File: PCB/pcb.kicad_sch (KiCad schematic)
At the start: 20 parts, among them J1 USB_C_Receptacle_USB2.0, SW1 SW_Push, U1 AT90USB1286-AU, Y1 Crystal_GND24_Small

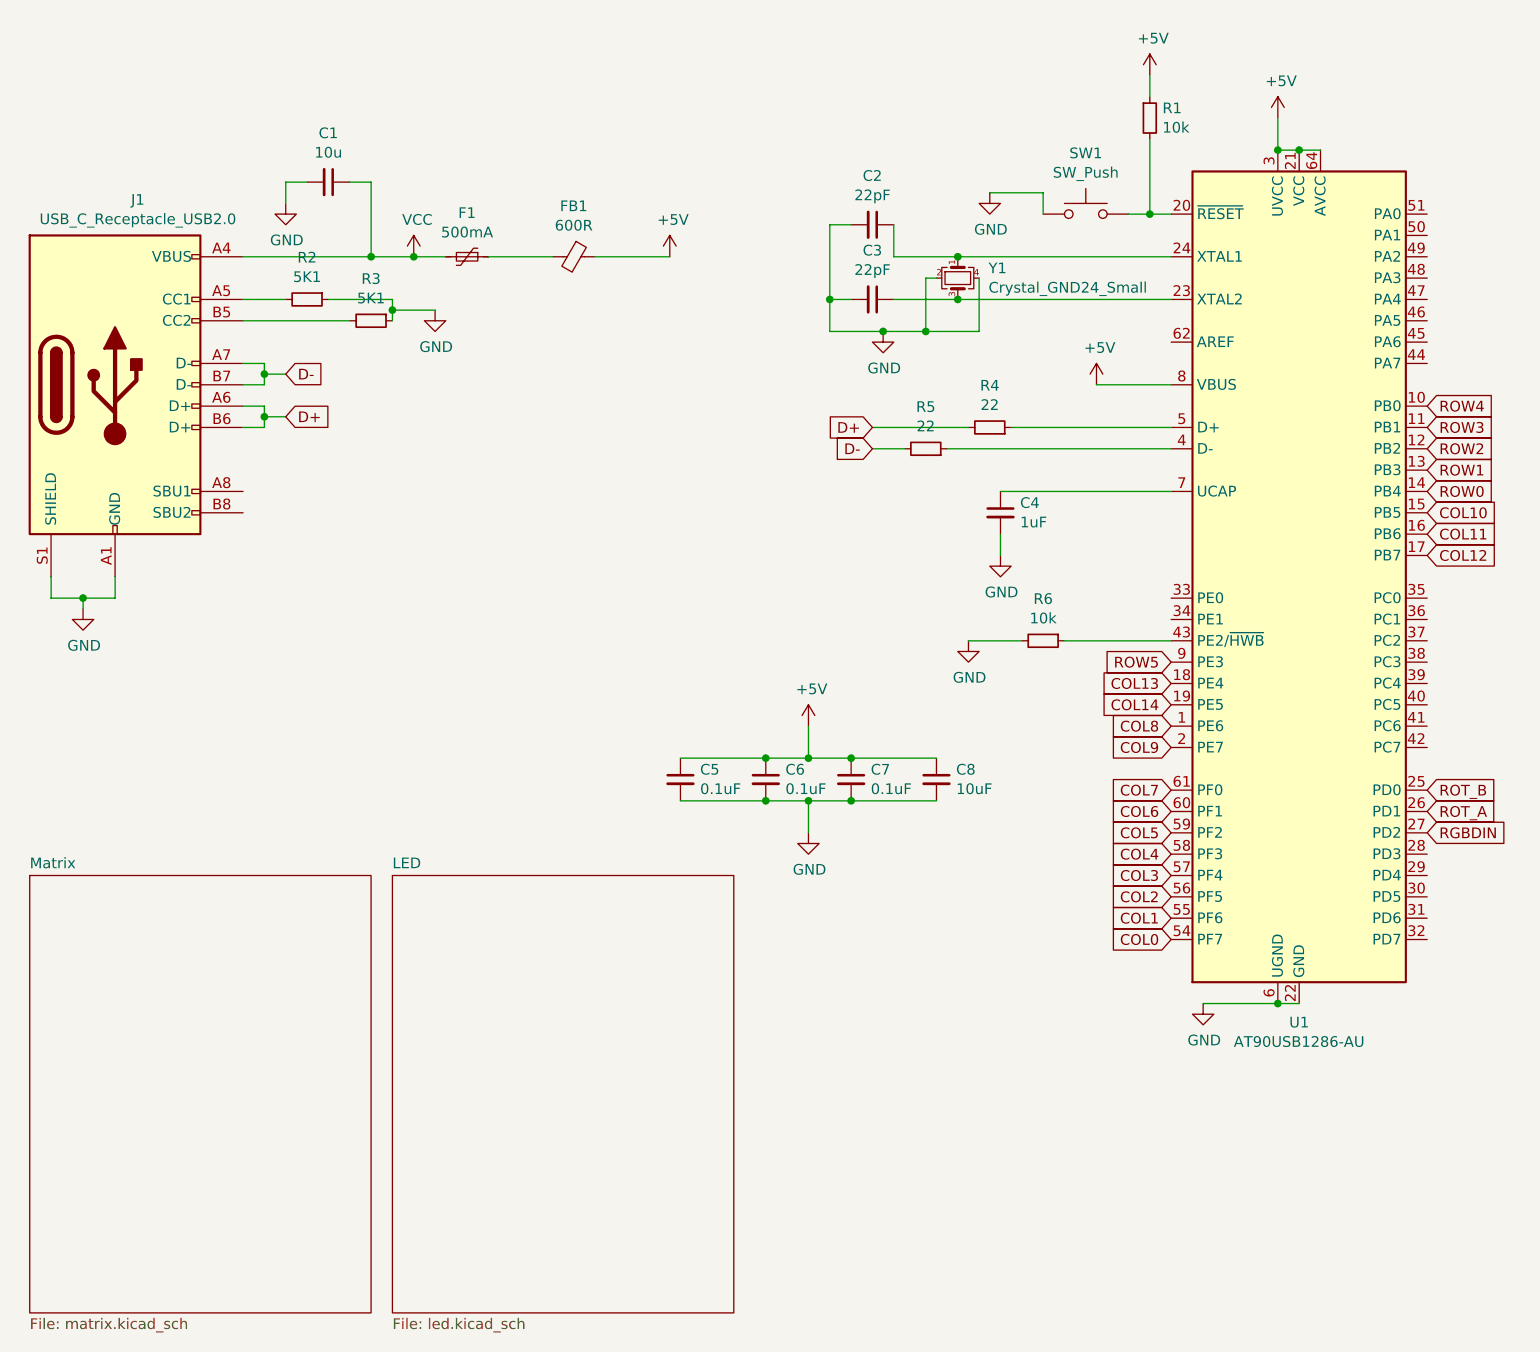
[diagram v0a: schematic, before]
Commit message: New Connector
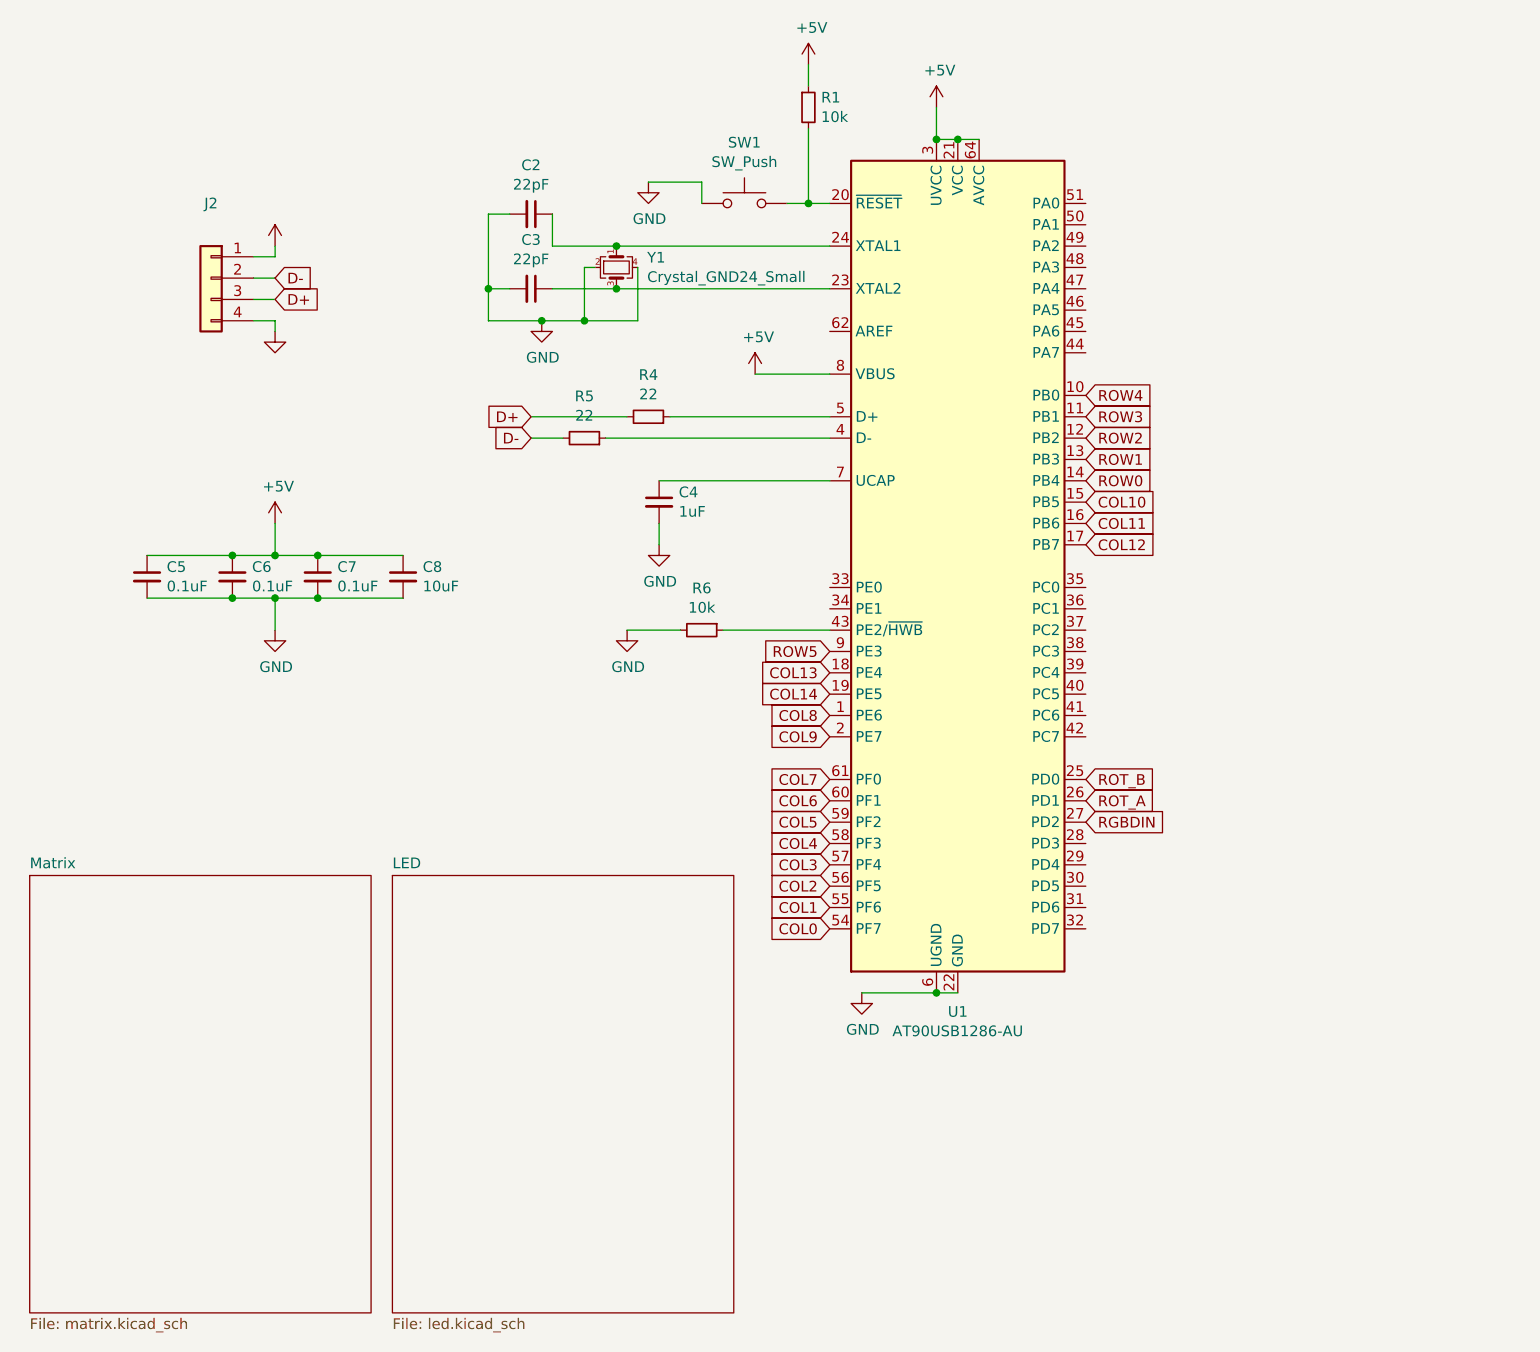
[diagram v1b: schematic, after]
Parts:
- removed C1: 10u, Capacitor_SMD:C_0805_2012Metric, symbol Device:C_Small
- removed F1: 500mA, symbol Device:Polyfuse_Small
- removed FB1: 600R, symbol pcb-rescue:Ferrite_Bead_Small-Device
- removed J1: USB_C_Receptacle_USB2.0, symbol pcb-rescue:USB_C_Receptacle_USB2.0-Connector
- removed R2, R3: 5K1, Resistor_SMD:R_0805_2012Metric, symbol Device:R_Small
- added J2: (no value), symbol Connector_Generic:Conn_01x04
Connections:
- net +5V: now also J2.1 (Pin_1)
- net D+: now also J2.3 (Pin_3)
- net D-: now also J2.2 (Pin_2)
- net GND: now also J2.4 (Pin_4)
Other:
- moved on the sheet: C2, C3, C4, C5, C6, C7, C8, R1, R4, R5, R6, SW1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

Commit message: Now only 2 alternative bottom rows
6.25U (Three 1U Keys to the right) and 7U (One 1.25U Key and one 1U Key to the right) Space Supported

Also new rounded PCB
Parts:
- J2: value (none) -> Conn_01x04; footprint (none) -> random-keyboard-parts:JST-SR-4
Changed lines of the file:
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@@
     (in_bom yes) (on_board yes) (fields_autoplaced)
     (property "Reference" "J2" (id 0) (at 38.1 38.1 0))
-    (property "Value" "" (id 1) (at 38.1 40.64 0))
-    (property "Footprint" "" (id 2) (at 38.1 46.99 0)
+    (property "Value" "Conn_01x04" (id 1) (at 38.1 40.64 0))
+    (property "Footprint" "random-keyboard-parts:JST-SR-4" (id 2) (at 38.1 46.99 0)
       (effects (font (size 1.27 1.27)) hide)
     )
@@
       (effects (font (size 1.27 1.27)) hide)
     )
-    (property "Value" "" (id 1) (at 45.72 38.1 0))
+    (property "Value" "+5V" (id 1) (at 45.72 38.1 0))
     (property "Footprint" "" (id 2) (at 45.72 43.18 0)
       (effects (font (size 1.27 1.27)) hide)
@@
       (effects (font (size 1.27 1.27)) hide)
     )
-    (property "Value" "" (id 1) (at 45.72 58.42 0))
+    (property "Value" "GND" (id 1) (at 45.72 58.42 0))
     (property "Footprint" "" (id 2) (at 45.72 53.34 0)
       (effects (font (size 1.27 1.27)) hide)
@@
     )
     (path "/f9b20734-b035-45c7-8e20-81df0eea752b/ab9a9193-8dcd-4cfc-a118-53936b727d37"
-      (reference "MX92") (unit 1) (value "MX-NoLED") (footprint "kailh-switches-hotswap:Kailh-Hotswap-6U-6.25U-7U")
+      (reference "MX92") (unit 1) (value "MX-NoLED") (footprint "kailh-switches-hotswap:Kailh-Hotswap-6.25U-7U")
     )
     (path "/f9b20734-b035-45c7-8e20-81df0eea752b/db04a73e-6619-49d9-a154-84655c6f4676"
-      (reference "MX93") (unit 1) (value "MX-NoLED") (footprint "kailh-switches-hotswap:Kailh-Hotswap-1U-1.25U")
+      (reference "MX93") (unit 1) (value "MX-NoLED") (footprint "kailh-switches-hotswap:Kailh-Hotswap-1U")
     )
     (path "/f9b20734-b035-45c7-8e20-81df0eea752b/75c11387-bc0f-40f0-8951-f94c4457e555"

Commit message: datalines and mosfet
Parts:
- added Q1: 2N7002, Package_TO_SOT_SMD:SOT-23, symbol Transistor_FET:2N7002
- added R2, R3: 10k, Resistor_SMD:R_0805_2012Metric, symbol Device:R_Small
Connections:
- net +5V: now also Q1.2 (S)
- net D+: now also R4.1, U1.5 (D+)
- net D-: now also R5.1, U1.4 (D-)
- net GND: now also R3.2
- net at U1.42 (PC7): now also R2.1
- new net: Q1.1 (G), R2.2, R3.1
- new net LED/led_5V: Q1.3 (D)
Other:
- sheet LED ports: added led_5V; removed none
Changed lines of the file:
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@@
   (junction (at 40.64 80.01) (diameter 0) (color 0 0 0 0)
   )
+  (junction (at 154.94 148.59) (diameter 0) (color 0 0 0 0)
+  )
   (junction (at 86.36 43.18) (diameter 0) (color 0 0 0 0)
   )
@@
     (stroke (width 0) (type default) (color 0 0 0 0))
   )
+  (wire (pts (xy 132.08 148.59) (xy 154.94 148.59))
+    (stroke (width 0) (type default) (color 0 0 0 0))
+  )
   (wire (pts (xy 127 30.48) (xy 124.46 30.48))
     (stroke (width 0) (type default) (color 0 0 0 0))
@@
     (stroke (width 0) (type default) (color 0 0 0 0))
   )
+  (wire (pts (xy 154.94 101.6) (xy 154.94 142.24))
+    (stroke (width 0) (type default) (color 0 0 0 0))
+  )
   (wire (pts (xy 71.12 52.07) (xy 77.47 52.07))
     (stroke (width 0) (type default) (color 0 0 0 0))
@@
     (stroke (width 0) (type default) (color 0 0 0 0))
   )
+  (wire (pts (xy 154.94 148.59) (xy 154.94 149.86))
+    (stroke (width 0) (type default) (color 0 0 0 0))
+  )
+  (wire (pts (xy 154.94 101.6) (xy 142.24 101.6))
+    (stroke (width 0) (type default) (color 0 0 0 0))
+  )
   (wire (pts (xy 30.48 80.01) (xy 40.64 80.01))
     (stroke (width 0) (type default) (color 0 0 0 0))
@@
     (stroke (width 0) (type default) (color 0 0 0 0))
   )
+  (wire (pts (xy 100.33 153.67) (xy 124.46 153.67))
+    (stroke (width 0) (type default) (color 0 0 0 0))
+  )
   (wire (pts (xy 87.63 63.5) (xy 76.2 63.5))
     (stroke (width 0) (type default) (color 0 0 0 0))
@@
     (stroke (width 0) (type default) (color 0 0 0 0))
   )
+  (wire (pts (xy 154.94 147.32) (xy 154.94 148.59))
+    (stroke (width 0) (type default) (color 0 0 0 0))
+  )
   (wire (pts (xy 40.64 85.09) (xy 45.72 85.09))
     (stroke (width 0) (type default) (color 0 0 0 0))
@@
   (wire (pts (xy 86.36 48.26) (xy 78.74 48.26))
     (stroke (width 0) (type default) (color 0 0 0 0))
+  )
+  (label "D+" (at 96.52 63.5 0)
+    (effects (font (size 1.27 1.27)) (justify left bottom))
+  )
+  (label "D-" (at 93.98 66.04 0)
+    (effects (font (size 1.27 1.27)) (justify left bottom))
   )
   (global_label "ROW2" (shape input) (at 142.24 66.04 0) (fields_autoplaced)
@@
     (pin "1")
   )
+  (symbol (lib_id "Device:R_Small") (at 154.94 152.4 0) (unit 1)
+    (in_bom yes) (on_board yes)
+    (property "Reference" "R3" (id 0) (at 149.9616 152.4 90))
+    (property "Value" "10k" (id 1) (at 152.273 152.4 90))
+    (property "Footprint" "Resistor_SMD:R_0805_2012Metric" (id 2) (at 154.94 152.4 0)
+      (effects (font (size 1.27 1.27)) hide)
+    )
+    (property "Datasheet" "~" (id 3) (at 154.94 152.4 0)
+      (effects (font (size 1.27 1.27)) hide)
+    )
+    (pin "1")
+    (pin "2")
+  )
+  (symbol (lib_id "power:+5V") (at 124.46 143.51 0) (unit 1)
+    (in_bom yes) (on_board yes)
+    (property "Reference" "#PWR0219" (id 0) (at 124.46 147.32 0)
+      (effects (font (size 1.27 1.27)) hide)
+    )
+    (property "Value" "+5V" (id 1) (at 127 142.24 0))
+    (property "Footprint" "" (id 2) (at 124.46 143.51 0)
+      (effects (font (size 1.27 1.27)) hide)
+    )
+    (property "Datasheet" "" (id 3) (at 124.46 143.51 0)
+      (effects (font (size 1.27 1.27)) hide)
+    )
+    (pin "1")
+  )
   (symbol (lib_id "Connector_Generic:Conn_01x04") (at 38.1 46.99 0) (mirror y) (unit 1)
     (in_bom yes) (on_board yes) (fields_autoplaced)
@@
     (pin "4")
   )
+  (symbol (lib_id "Device:R_Small") (at 154.94 144.78 0) (unit 1)
+    (in_bom yes) (on_board yes)
+    (property "Reference" "R2" (id 0) (at 149.9616 144.78 90))
+    (property "Value" "10k" (id 1) (at 152.273 144.78 90))
+    (property "Footprint" "Resistor_SMD:R_0805_2012Metric" (id 2) (at 154.94 144.78 0)
+      (effects (font (size 1.27 1.27)) hide)
+    )
+    (property "Datasheet" "~" (id 3) (at 154.94 144.78 0)
+      (effects (font (size 1.27 1.27)) hide)
+    )
+    (pin "1")
+    (pin "2")
+  )
+  (symbol (lib_id "power:GND") (at 154.94 154.94 0) (unit 1)
+    (in_bom yes) (on_board yes)
+    (property "Reference" "#PWR0220" (id 0) (at 154.94 161.29 0)
+      (effects (font (size 1.27 1.27)) hide)
+    )
+    (property "Value" "GND" (id 1) (at 155.067 159.3342 0))
+    (property "Footprint" "" (id 2) (at 154.94 154.94 0)
+      (effects (font (size 1.27 1.27)) hide)
+    )
+    (property "Datasheet" "" (id 3) (at 154.94 154.94 0)
+      (effects (font (size 1.27 1.27)) hide)
+    )
+    (pin "1")
+  )
   (symbol (lib_id "power:+5V") (at 45.72 43.18 0) (unit 1)
     (in_bom yes) (on_board yes) (fields_autoplaced)
@@
     )
     (pin "1")
+  )
+  (symbol (lib_id "Transistor_FET:2N7002") (at 127 148.59 180) (unit 1)
+    (in_bom yes) (on_board yes) (fields_autoplaced)
+    (property "Reference" "Q1" (id 0) (at 120.65 147.3199 0)
+      (effects (font (size 1.27 1.27)) (justify left))
+    )
+    (property "Value" "2N7002" (id 1) (at 120.65 149.8599 0)
+      (effects (font (size 1.27 1.27)) (justify left))
+    )
+    (property "Footprint" "Package_TO_SOT_SMD:SOT-23" (id 2) (at 121.92 146.685 0)
+      (effects (font (size 1.27 1.27) italic) (justify left) hide)
+    )
+    (property "Datasheet" "https://www.onsemi.com/pub/Collateral/NDS7002A-D.PDF" (id 3) (at 127 148.59 0)
+      (effects (font (size 1.27 1.27)) (justify left) hide)
+    )
+    (pin "1")
+    (pin "2")
+    (pin "3")
   )
   (sheet (at 59.69 118.11) (size 40.64 52.07) (fields_autoplaced)
@@
       (effects (font (size 1.27 1.27)) (justify left top))
     )
+    (pin "led_5V" input (at 100.33 153.67 0)
+      (effects (font (size 1.27 1.27)) (justify right))
+    )
   )
   (sheet (at 16.51 118.11) (size 40.64 52.07) (fields_autoplaced)
@@
       (reference "#PWR015") (unit 1) (value "GND") (footprint "")
     )
-    (path "/d6d52913-7ca3-461f-9b21-a792e8c1de6f/595a69f7-6e5e-41d9-a0e8-0cbb5f30019a"
-      (reference "#PWR016") (unit 1) (value "+5V") (footprint "")
-    )
-    (path "/d6d52913-7ca3-461f-9b21-a792e8c1de6f/ff6ab37a-ff62-48ff-b3c5-4438ebb9e0ae"
-      (reference "#PWR017") (unit 1) (value "+5V") (footprint "")
-    )
-    (path "/d6d52913-7ca3-461f-9b21-a792e8c1de6f/18325703-e457-4017-b1e6-02001a64410b"
-      (reference "#PWR018") (unit 1) (value "+5V") (footprint "")
-    )
-    (path "/d6d52913-7ca3-461f-9b21-a792e8c1de6f/367102c9-88a2-4677-a8a4-4d627e628848"
-      (reference "#PWR019") (unit 1) (value "+5V") (footprint "")
-    )
-    (path "/d6d52913-7ca3-461f-9b21-a792e8c1de6f/2f372785-65be-4247-a238-a3bd661c1519"
-      (reference "#PWR020") (unit 1) (value "+5V") (footprint "")
-    )
-    (path "/d6d52913-7ca3-461f-9b21-a792e8c1de6f/5f285571-b571-44b6-9006-b704aa14215c"
-      (reference "#PWR021") (unit 1) (value "+5V") (footprint "")
-    )
-    (path "/d6d52913-7ca3-461f-9b21-a792e8c1de6f/5cfce0c3-d372-41a9-955d-94eeb2d35a9c"
-      (reference "#PWR022") (unit 1) (value "+5V") (footprint "")
-    )
-    (path "/d6d52913-7ca3-461f-9b21-a792e8c1de6f/85e1ed5c-60ee-47c5-b0ef-83e9908b74d5"
-      (reference "#PWR023") (unit 1) (value "+5V") (footprint "")
-    )
-    (path "/d6d52913-7ca3-461f-9b21-a792e8c1de6f/8fbbc132-deae-4f7c-9b91-0fef32de507c"
-      (reference "#PWR024") (unit 1) (value "+5V") (footprint "")
-    )
-    (path "/d6d52913-7ca3-461f-9b21-a792e8c1de6f/a93014bb-5128-4bc4-ad13-54deeb2e514f"
-      (reference "#PWR025") (unit 1) (value "+5V") (footprint "")
-    )
     (path "/d6d52913-7ca3-461f-9b21-a792e8c1de6f/4e714991-e30b-499c-bfd0-9293f556ef91"
       (reference "#PWR026") (unit 1) (value "GND") (footprint "")
@@
       (reference "#PWR0218") (unit 1) (value "GND") (footprint "")
     )
+    (path "/2f7574c6-eb03-4e03-84aa-f313010a2952"
+      (reference "#PWR0219") (unit 1) (value "+5V") (footprint "")
+    )
+    (path "/8b282440-588c-48fa-870c-51fcb1aad6da"
+      (reference "#PWR0220") (unit 1) (value "GND") (footprint "")
+    )
     (path "/00000000-0000-0000-0000-00006225d90c"
       (reference "C2") (unit 1) (value "22pF") (footprint "Capacitor_SMD:C_0805_2012Metric")
@@
       (reference "MX100") (unit 1) (value "MX-NoLED") (footprint "kailh-switches-hotswap:Kailh-Hotswap-1U")
     )
+    (path "/ffcf6f9b-ad9c-401f-a1ca-cca200e68ad6"
+      (reference "Q1") (unit 1) (value "2N7002") (footprint "Package_TO_SOT_SMD:SOT-23")
+    )
     (path "/00000000-0000-0000-0000-00006226a5d7"
       (reference "R1") (unit 1) (value "10k") (footprint "Resistor_SMD:R_0805_2012Metric")
     )
+    (path "/71dc84d4-9b14-483e-8a4c-98052e279284"
+      (reference "R2") (unit 1) (value "10k") (footprint "Resistor_SMD:R_0805_2012Metric")
+    )
+    (path "/2d3b7a5b-300a-403f-bb8d-18aef7951f08"
+      (reference "R3") (unit 1) (value "10k") (footprint "Resistor_SMD:R_0805_2012Metric")
+    )
     (path "/00000000-0000-0000-0000-00006224f059"

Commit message: change port position
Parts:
- added R7: (no value), symbol Device:R_Small
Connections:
- net +5V: now also R7.2; no longer J2.1 (Pin_1)
- net RGBDIN renamed LED/RGB_Data
- new net: J2.1 (Pin_1), R7.1
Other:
- sheet LED ports: added RGB_Data; removed none
- moved on the sheet: Q1, R2, R3
